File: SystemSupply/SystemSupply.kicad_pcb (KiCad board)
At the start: 2 copper layers, 75 x 75 mm, 52 parts, among them J1 Conn_01x01, J10 Screw_Terminal_01x02, J2 Conn_01x01, J3 4P4C, J4 Conn_01x01, J5 Conn_01x01, J6 Screw_Terminal_01x02, J7 4P4C, J8 Screw_Terminal_01x02, J9 Screw_Terminal_01x02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

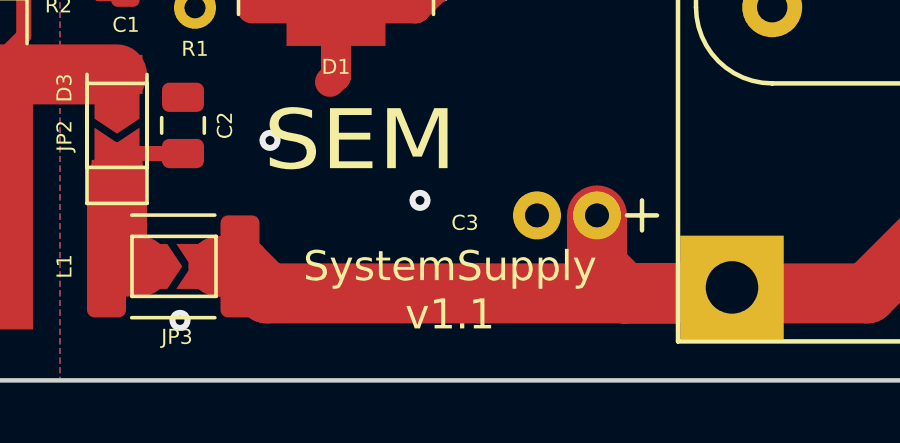
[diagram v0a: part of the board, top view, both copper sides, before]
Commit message: Changed 1.1 to 1.0 versions.
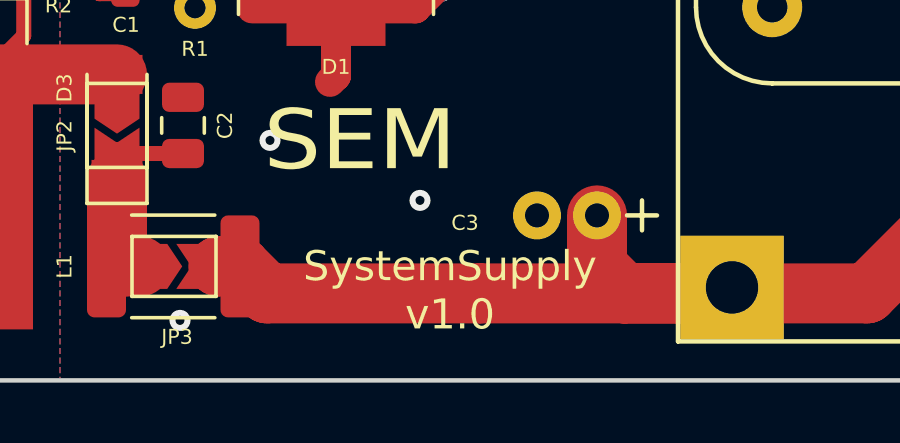
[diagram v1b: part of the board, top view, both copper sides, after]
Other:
- board text added: "SystemSupply v1.0"
- board text removed: "SystemSupply v1.1"
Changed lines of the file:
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@@
     )
   )
-  (gr_text "SystemSupply\nv1.1" (at 99 162) (layer F.SilkS)
+  (gr_text "SystemSupply\nv1.0" (at 99 162) (layer F.SilkS)
     (effects (font (size 1 1) (thickness 0.2)))
   )

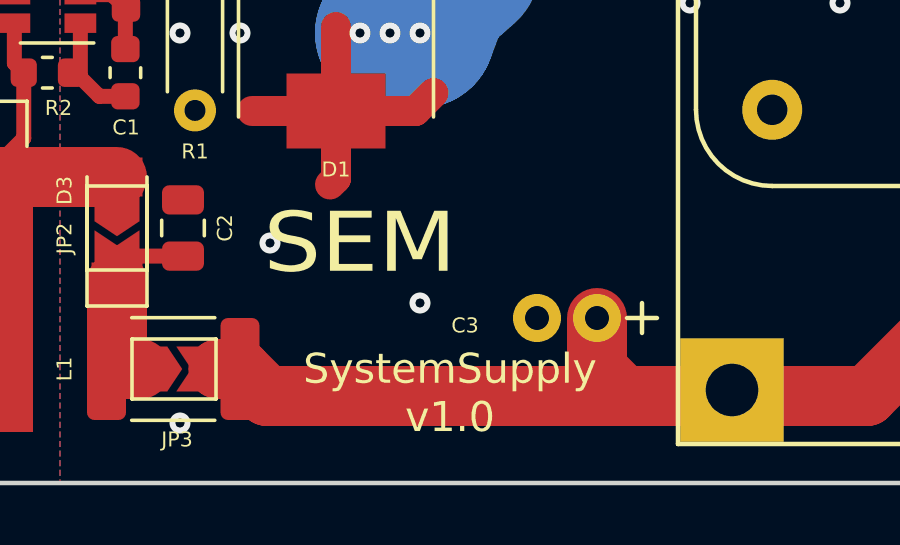
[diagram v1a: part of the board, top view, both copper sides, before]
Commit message: Added version date on silk screen and changed signal tracks width to 0,2.
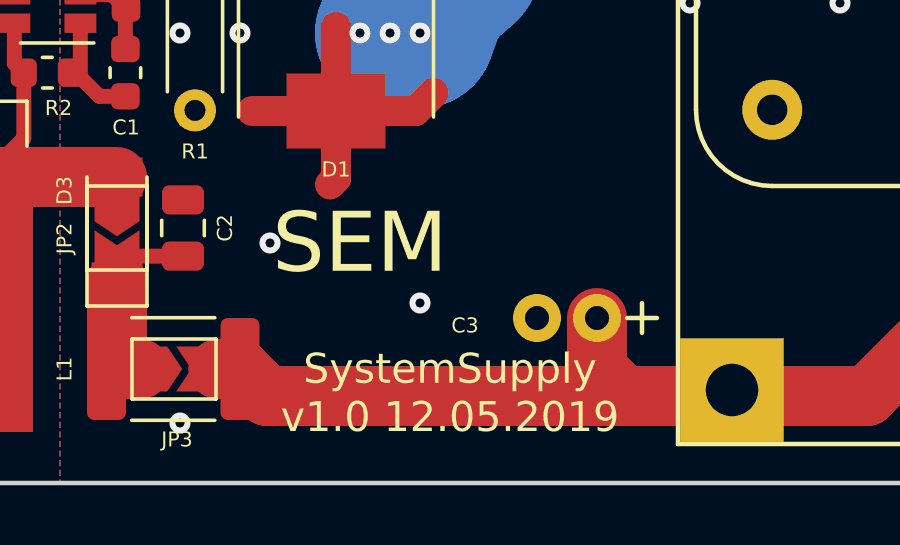
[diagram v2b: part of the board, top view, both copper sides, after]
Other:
- board text added: "SystemSupply v1.0 12.05.2019"
- board text removed: "SystemSupply v1.0"
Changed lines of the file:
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@@
     (user_trace_width 5)
     (trace_clearance 0.2)
-    (zone_clearance 0.508)
+    (zone_clearance 0.2)
     (zone_45_only no)
     (trace_min 0.2)
@@
     )
   )
-  (gr_text "SystemSupply\nv1.0" (at 99 162) (layer F.SilkS)
+  (gr_text "SystemSupply\nv1.0 12.05.2019" (at 99 162) (layer F.SilkS)
     (effects (font (size 1 1) (thickness 0.2)))
   )
@@
   )
   (gr_text SEM (at 96 157) (layer F.SilkS)
-    (effects (font (size 2 2.2) (thickness 0.25)))
+    (effects (font (size 2 2) (thickness 0.3)))
   )
   (gr_text FC (at 86.6 106.4 90) (layer F.SilkS)
@@
   (segment (start 116.2 111.6) (end 120.9 111.6) (width 2) (layer B.Cu) (net 27))
   (zone (net 4) (net_name GND) (layer F.Cu) (hatch edge 0.508)
-    (connect_pads (clearance 0.25))
-    (min_thickness 0.25)
-    (fill yes (arc_segments 16) (thermal_gap 0.3) (thermal_bridge_width 0.4))
+    (connect_pads (clearance 0.2))
+    (min_thickness 0.2)
+    (fill yes (arc_segments 16) (thermal_gap 0.2) (thermal_bridge_width 0.4))
     (polygon
       (pts
@@
   )
   (zone (net 4) (net_name GND) (layer B.Cu) (hatch edge 0.508)
-    (connect_pads (clearance 0.25))
-    (min_thickness 0.25)
-    (fill yes (arc_segments 16) (thermal_gap 0.3) (thermal_bridge_width 0.4))
+    (connect_pads (clearance 0.2))
+    (min_thickness 0.2)
+    (fill yes (arc_segments 16) (thermal_gap 0.2) (thermal_bridge_width 0.4))
     (polygon
       (pts
